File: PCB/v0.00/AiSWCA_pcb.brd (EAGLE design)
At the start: 100 x 80 mm, 24 parts, among them IC1 LM1117IMPX-3.3, IC2 AD8400R, T1 BC847

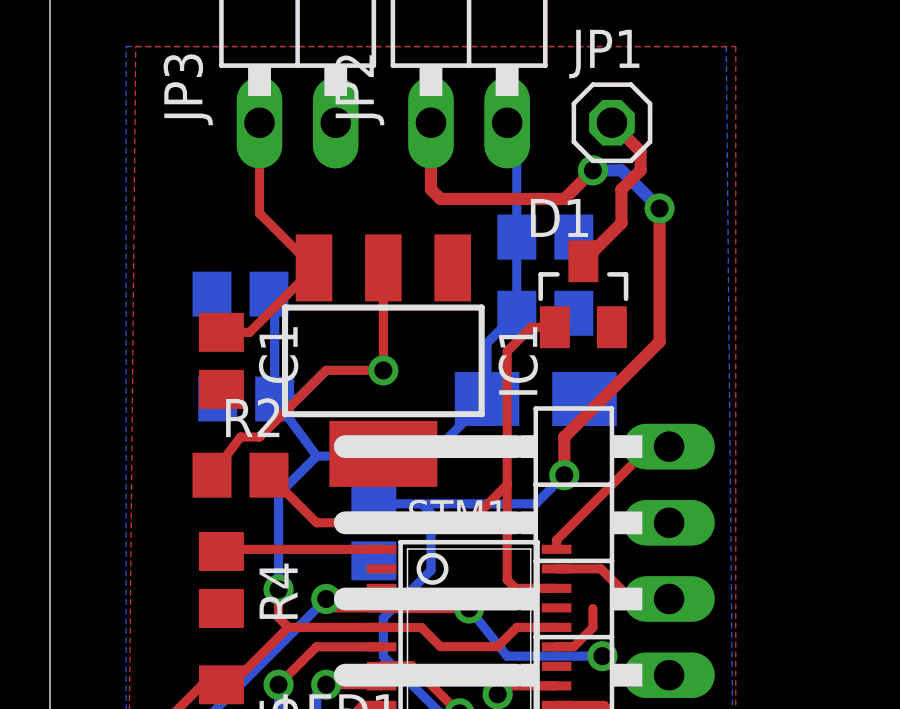
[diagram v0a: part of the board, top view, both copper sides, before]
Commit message: Replaced previous Schottky diode with one in SOD323 package.
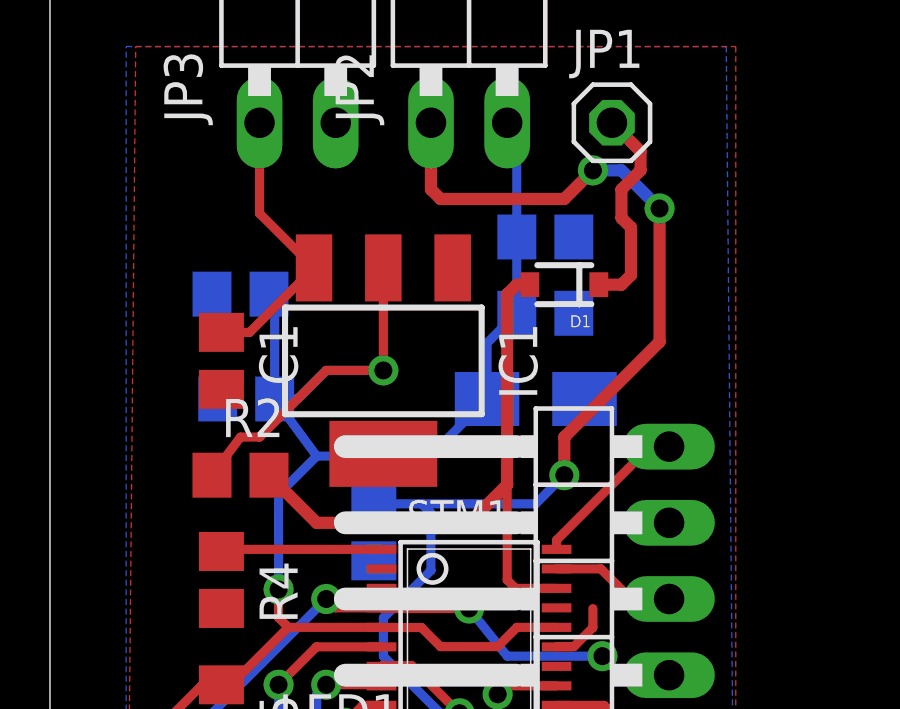
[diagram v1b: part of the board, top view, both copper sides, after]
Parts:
- D1: value BAT54 -> PMEG4005EJ; device diode:SOT23 -> SparkFun-DiscreteSemi:SOD-323
- moved D1 0.71 mm to (17.1, 37.1), turned to 180 degrees
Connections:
- net N$3: now also D1.C; no longer D1.3
- net USART1_RX: now also D1.A; no longer D1.1
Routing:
- net N$3: track 5.80 -> 7.07 mm
- net USART1_RX: track 20.4 -> 21.3 mm
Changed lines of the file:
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@@
 <layer number="54" name="bGND_GNDA" color="7" fill="1" visible="yes" active="yes"/>
 <layer number="56" name="wert" color="7" fill="1" visible="yes" active="yes"/>
+<layer number="57" name="tCAD" color="7" fill="1" visible="no" active="no"/>
+<layer number="59" name="tCarbon" color="7" fill="1" visible="no" active="no"/>
+<layer number="60" name="bCarbon" color="7" fill="1" visible="no" active="no"/>
+<layer number="90" name="Modules" color="5" fill="1" visible="no" active="no"/>
 <layer number="91" name="Nets" color="2" fill="1" visible="no" active="no"/>
 <layer number="92" name="Busses" color="1" fill="1" visible="no" active="no"/>
@@
 <layer number="109" name="fp9" color="7" fill="1" visible="yes" active="yes"/>
 <layer number="110" name="fp0" color="7" fill="1" visible="yes" active="yes"/>
+<layer number="111" name="LPC17xx" color="7" fill="1" visible="yes" active="yes"/>
+<layer number="112" name="tSilk" color="7" fill="1" visible="yes" active="yes"/>
+<layer number="113" name="IDFDebug" color="7" fill="1" visible="yes" active="yes"/>
 <layer number="116" name="Patch_BOT" color="7" fill="1" visible="yes" active="yes"/>
+<layer number="118" name="Rect_Pads" color="7" fill="1" visible="yes" active="yes"/>
 <layer number="121" name="tTestdril" color="7" fill="1" visible="yes" active="yes"/>
 <layer number="122" name="bTestdril" color="7" fill="1" visible="yes" active="yes"/>
 <layer number="123" name="tTestmark" color="7" fill="1" visible="yes" active="yes"/>
 <layer number="124" name="bTestmark" color="7" fill="1" visible="yes" active="yes"/>
+<layer number="125" name="_tNames" color="7" fill="1" visible="yes" active="yes"/>
+<layer number="126" name="_bNames" color="7" fill="1" visible="yes" active="yes"/>
+<layer number="127" name="_tValues" color="7" fill="1" visible="yes" active="yes"/>
+<layer number="128" name="_bValues" color="7" fill="1" visible="yes" active="yes"/>
+<layer number="129" name="Mask" color="7" fill="1" visible="yes" active="yes"/>
 <layer number="131" name="tAdjust" color="7" fill="1" visible="yes" active="yes"/>
 <layer number="132" name="bAdjust" color="7" fill="1" visible="yes" active="yes"/>
+<layer number="144" name="Drill_legend" color="7" fill="1" visible="yes" active="yes"/>
+<layer number="150" name="Notes" color="7" fill="1" visible="yes" active="yes"/>
 <layer number="151" name="HeatSink" color="7" fill="1" visible="yes" active="yes"/>
+<layer number="152" name="_bDocu" color="7" fill="1" visible="yes" active="yes"/>
+<layer number="153" name="FabDoc1" color="7" fill="1" visible="yes" active="yes"/>
+<layer number="154" name="FabDoc2" color="7" fill="1" visible="yes" active="yes"/>
+<layer number="155" name="FabDoc3" color="7" fill="1" visible="yes" active="yes"/>
+<layer number="199" name="Contour" color="7" fill="1" visible="yes" active="yes"/>
 <layer number="200" name="200bmp" color="1" fill="10" visible="no" active="no"/>
 <layer number="201" name="201bmp" color="7" fill="1" visible="yes" active="yes"/>
@@
 <layer number="230" name="230bmp" color="7" fill="1" visible="yes" active="yes"/>
 <layer number="231" name="231bmp" color="7" fill="1" visible="yes" active="yes"/>
+<layer number="248" name="Housing" color="7" fill="1" visible="yes" active="yes"/>
+<layer number="249" name="Edge" color="7" fill="1" visible="yes" active="yes"/>
 <layer number="250" name="Descript" color="3" fill="1" visible="no" active="no"/>
 <layer number="251" name="SMDround" color="12" fill="11" visible="no" active="no"/>
 <layer number="254" name="OrgLBR" color="7" fill="1" visible="yes" active="yes"/>
+<layer number="255" name="routoute" color="7" fill="1" visible="yes" active="yes"/>
 </layers>
 <board>
@@
 <attribute name="OC_FARNELL" value="unknown" x="16.51" y="13.97" size="1.778" layer="27" rot="R180" display="off"/>
 </element>
-<element name="D1" library="diode" package="SOT23" value="BAT54" x="17.78" y="36.83"/>
+<element name="D1" library="SparkFun-DiscreteSemi" package="SOD-323" value="PMEG4005EJ" x="17.145" y="37.1475" rot="R180">
+<attribute name="VALUE" value="PMEG4005EJ" x="17.145" y="37.1475" size="1.778" layer="27" rot="R180" display="off"/>
+<attribute name="PROD_ID" value="DIO-10955" x="17.145" y="37.1475" size="1.778" layer="27" rot="R180" display="off"/>
+</element>
 <element name="R2" library="rcl" package="R0805" value="10k" x="6.35" y="30.7975"/>
 <element name="IC2" library="00_koarl-div" package="SO8" value="AD8400R" x="15.5575" y="18.7325" rot="R90"/>
@@
 <contactref element="STM1" pad="18"/>
 <contactref element="R2" pad="2"/>
-<contactref element="D1" pad="1"/>
+<contactref element="D1" pad="A"/>
 <wire x1="16.8878" y1="27.025" x2="15.52" y2="27.025" width="0.3048" layer="1"/>
 <wire x1="15.52" y1="27.025" x2="15.24" y2="27.305" width="0.3048" layer="1"/>
 <wire x1="15.24" y1="27.305" x2="15.24" y2="30.48" width="0.3048" layer="1"/>
-<wire x1="15.24" y1="30.48" x2="15.24" y2="34.925" width="0.3048" layer="1"/>
-<wire x1="7.3" y1="30.7975" x2="8.89" y2="29.21" width="0.3048" layer="1"/>
-<wire x1="8.89" y1="29.21" x2="13.97" y2="29.21" width="0.3048" layer="1"/>
-<wire x1="13.97" y1="29.21" x2="15.24" y2="30.48" width="0.3048" layer="1"/>
-<wire x1="15.24" y1="34.925" x2="16.045" y2="35.73" width="0.3048" layer="1"/>
-<wire x1="16.045" y1="35.73" x2="16.83" y2="35.73" width="0.3048" layer="1"/>
+<wire x1="15.24" y1="36.83" x2="15.5575" y2="37.1475" width="0.4064" layer="1"/>
+<wire x1="15.5575" y1="37.1475" x2="15.995" y2="37.1475" width="0.4064" layer="1"/>
+<wire x1="15.24" y1="36.83" x2="15.24" y2="30.48" width="0.4064" layer="1"/>
+<wire x1="15.24" y1="30.48" x2="13.97" y2="29.21" width="0.4064" layer="1"/>
+<wire x1="13.97" y1="29.21" x2="8.8875" y2="29.21" width="0.4064" layer="1"/>
+<wire x1="8.8875" y1="29.21" x2="7.3" y2="30.7975" width="0.4064" layer="1"/>
 </signal>
 <signal name="SPI_MOSI">
@@
 </signal>
 <signal name="N$3">
-<contactref element="D1" pad="3"/>
+<contactref element="D1" pad="C"/>
 <contactref element="JP1" pad="1"/>
 <wire x1="18.7325" y1="42.545" x2="19.685" y2="41.5925" width="0.4064" layer="1"/>
 <wire x1="19.685" y1="41.5925" x2="19.685" y2="40.9575" width="0.4064" layer="1"/>
 <wire x1="19.685" y1="40.9575" x2="19.05" y2="40.3225" width="0.4064" layer="1"/>
-<wire x1="19.05" y1="40.3225" x2="19.05" y2="39.2" width="0.4064" layer="1"/>
-<wire x1="19.05" y1="39.2" x2="17.78" y2="37.93" width="0.4064" layer="1"/>
+<wire x1="19.05" y1="40.3225" x2="19.05" y2="39.37" width="0.4064" layer="1"/>
+<wire x1="19.05" y1="39.37" x2="19.3675" y2="39.0525" width="0.4064" layer="1"/>
+<wire x1="19.3675" y1="39.0525" x2="19.3675" y2="37.465" width="0.4064" layer="1"/>
+<wire x1="19.3675" y1="37.465" x2="19.05" y2="37.1475" width="0.4064" layer="1"/>
+<wire x1="19.05" y1="37.1475" x2="18.295" y2="37.1475" width="0.4064" layer="1"/>
 </signal>
 <signal name="SPI_CS">

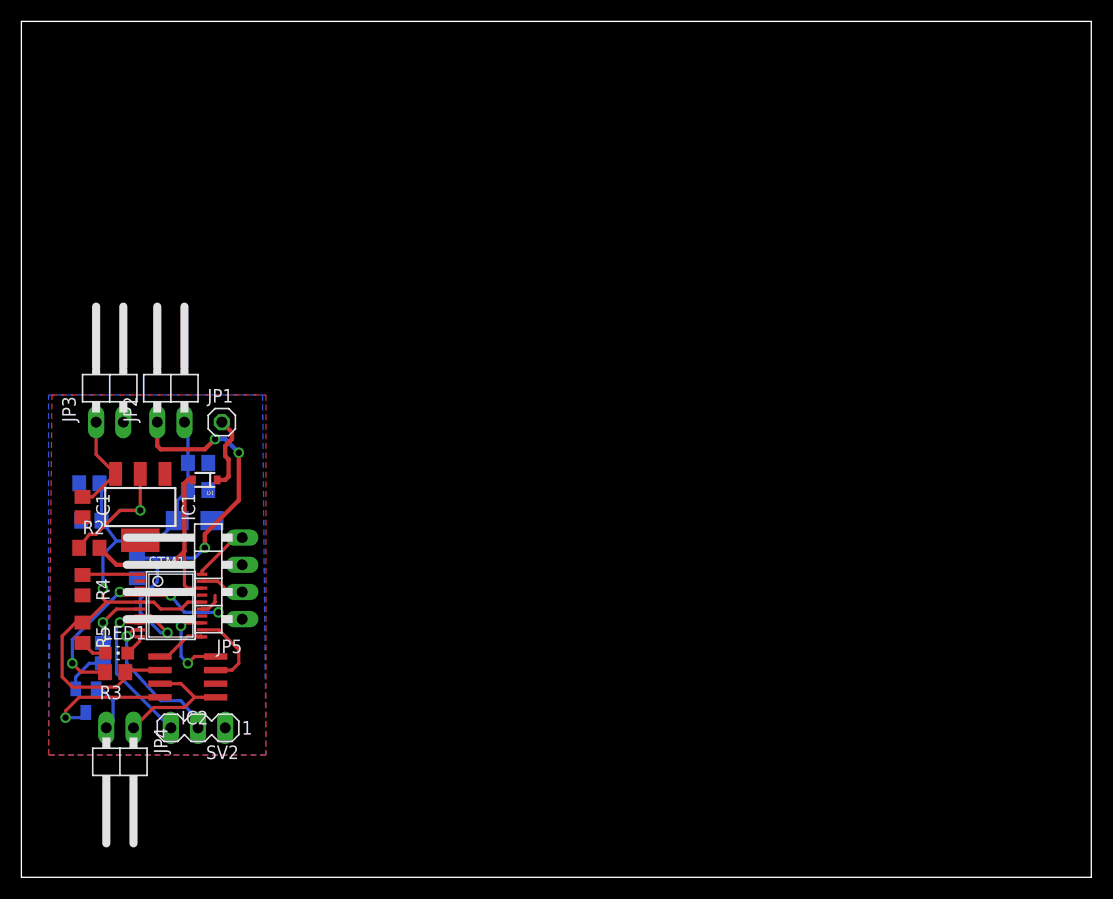
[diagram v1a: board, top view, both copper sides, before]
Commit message: Added diode (SOD323 package) on power section
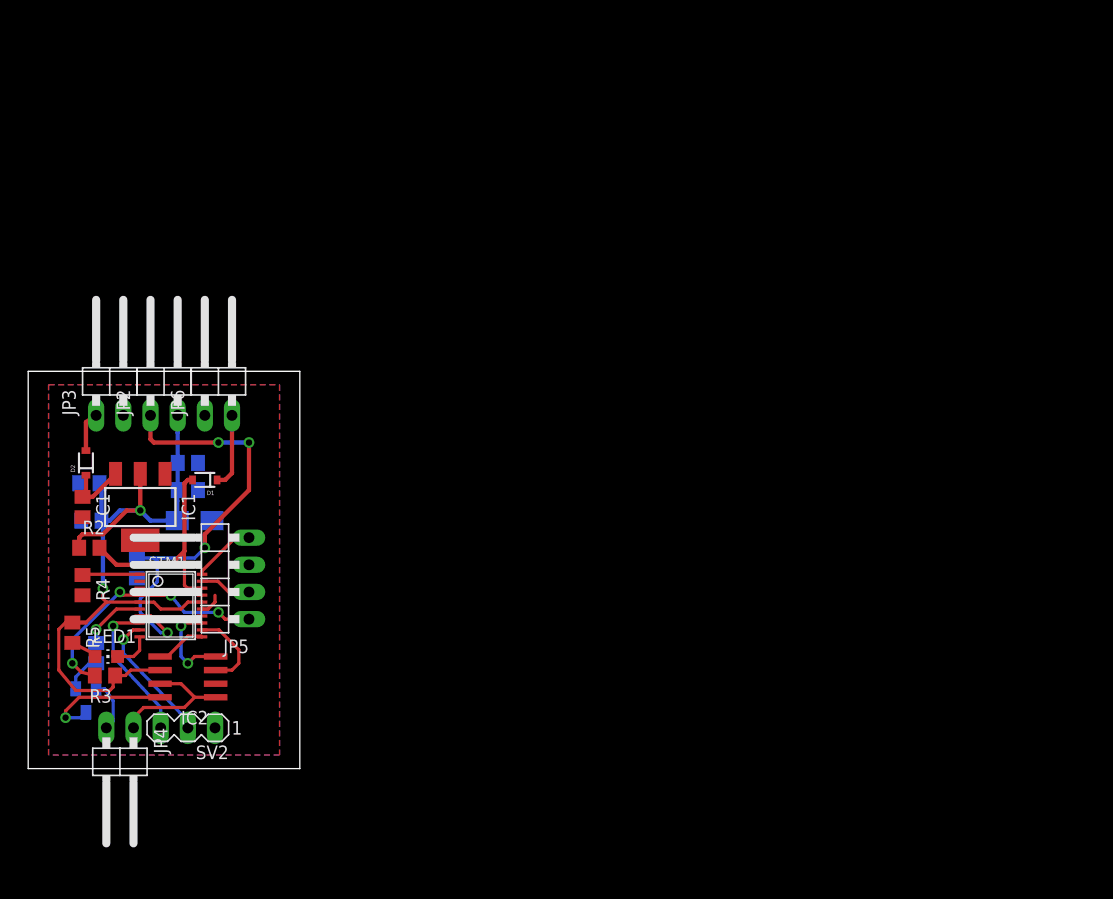
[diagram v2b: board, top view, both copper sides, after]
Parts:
- removed JP1: K-Bus, pinhead:1X01
- added D2: PMEG4005EJ, SparkFun-DiscreteSemi:SOD-323
- added JP6: K-Bus, pinhead:1X02/90
- moved LED1 1.00 mm to (7.94, 20.6)
- moved R3 1.00 mm to (7.81, 18.9)
- moved C2 0.95 mm to (15.6, 38.7)
- moved C4 0.95 mm to (15.6, 36.2)
- moved SV2 0.95 mm to (15.6, 14.0)
- moved R5 0.95 mm to (4.76, 22.9)
- moved JP2 0.90 mm to (13.3, 47.0)
- moved JP3 0.64 mm to (8.26, 47.0)
- moved R6 0.63 mm to (6.99, 21.0)
- moved JP5 0.63 mm to (17.5, 27.9)
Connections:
- new net N$4: D2.A, JP3.1
- net N$1: now also D2.C; no longer JP3.1
- net N$3: now also JP6.2; no longer JP1.1
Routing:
- net N$4: track 0.00 -> 3.80 mm
- net N$1: track 9.57 -> 6.45 mm
- net ADC_IN1: track 40.3 -> 42.3 mm
- net N$5: track 1.98 -> 3.57 mm
- net VCC: track 72.9 -> 71.6 mm
- net USART2_RX: track 13.7 -> 12.6 mm
- net N$14: track 4.51 -> 3.55 mm
- net SWDIO: track 4.17 -> 4.80 mm
- net N$12: track 12.6 -> 13.2 mm
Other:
- board size 100 x 80 mm -> 25.4 x 37.1 mm

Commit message: Added values to some of elements on schematics.
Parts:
- C1: value (none) -> 10u
- C2: value (none) -> 100u
- R3: value (none) -> 100k
- R4: value (none) -> 10k
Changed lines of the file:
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@@
 <layers>
 <layer number="1" name="Top" color="4" fill="1" visible="no" active="yes"/>
-<layer number="16" name="Bottom" color="1" fill="1" visible="no" active="yes"/>
-<layer number="17" name="Pads" color="2" fill="1" visible="no" active="yes"/>
-<layer number="18" name="Vias" color="2" fill="1" visible="no" active="yes"/>
+<layer number="16" name="Bottom" color="1" fill="1" visible="yes" active="yes"/>
+<layer number="17" name="Pads" color="2" fill="1" visible="yes" active="yes"/>
+<layer number="18" name="Vias" color="2" fill="1" visible="yes" active="yes"/>
 <layer number="19" name="Unrouted" color="6" fill="1" visible="no" active="yes"/>
-<layer number="20" name="Dimension" color="15" fill="1" visible="no" active="yes"/>
+<layer number="20" name="Dimension" color="15" fill="1" visible="yes" active="yes"/>
 <layer number="21" name="tPlace" color="7" fill="1" visible="no" active="yes"/>
-<layer number="22" name="bPlace" color="7" fill="1" visible="no" active="yes"/>
+<layer number="22" name="bPlace" color="7" fill="1" visible="yes" active="yes"/>
 <layer number="23" name="tOrigins" color="15" fill="1" visible="no" active="yes"/>
-<layer number="24" name="bOrigins" color="15" fill="1" visible="no" active="yes"/>
-<layer number="25" name="tNames" color="7" fill="1" visible="yes" active="yes"/>
+<layer number="24" name="bOrigins" color="15" fill="1" visible="yes" active="yes"/>
+<layer number="25" name="tNames" color="7" fill="1" visible="no" active="yes"/>
 <layer number="26" name="bNames" color="7" fill="1" visible="yes" active="yes"/>
 <layer number="27" name="tValues" color="7" fill="1" visible="no" active="yes"/>
@@
 <elements>
 <element name="STM1" library="stm32f030f4" package="TSSOP20" value="STM32F070F6P6" x="13.97" y="25.4" rot="R270"/>
-<element name="R4" library="rcl" package="R0805" value="" x="5.715" y="27.305" rot="R270"/>
-<element name="R3" library="rcl" package="R0805" value="" x="7.8105" y="18.8595" rot="R180"/>
+<element name="R4" library="rcl" package="R0805" value="10k" x="5.715" y="27.305" rot="R270"/>
+<element name="R3" library="rcl" package="R0805" value="100k" x="7.8105" y="18.8595" rot="R180"/>
 <element name="C3" library="rcl" package="C0805" value="" x="6.5405" y="33.3375" rot="MR0"/>
 <element name="C4" library="rcl" package="C0805" value="" x="15.5575" y="36.195" rot="MR180"/>
@@
 <element name="JP3" library="pinhead" package="1X02/90" value="PWR" x="8.255" y="46.99"/>
 <element name="IC1" library="lm1117" package="SOT223" value="LM1117IMPX-3.3" x="11.1125" y="34.6075" rot="R180"/>
-<element name="C1" library="rcl" package="C0805" value="" x="5.715" y="34.6075" rot="R270"/>
-<element name="C2" library="rcl" package="C0805" value="" x="15.5575" y="38.735" rot="MR180"/>
+<element name="C1" library="rcl" package="C0805" value="10u" x="5.715" y="34.6075" rot="R270"/>
+<element name="C2" library="rcl" package="C0805" value="100u" x="15.5575" y="38.735" rot="MR180"/>
 <element name="SV2" library="con-lstb" package="MA03-1" value="Debug" x="15.5575" y="13.97" rot="R180">
 <attribute name="OC_NEWARK" value="unknown" x="15.5575" y="13.97" size="1.778" layer="27" rot="R180" display="off"/>
